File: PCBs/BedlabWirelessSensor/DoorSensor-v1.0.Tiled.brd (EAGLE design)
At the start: 43.2 x 51.1 mm, 19 parts, among them U1 ATMEGA328P_PDIP

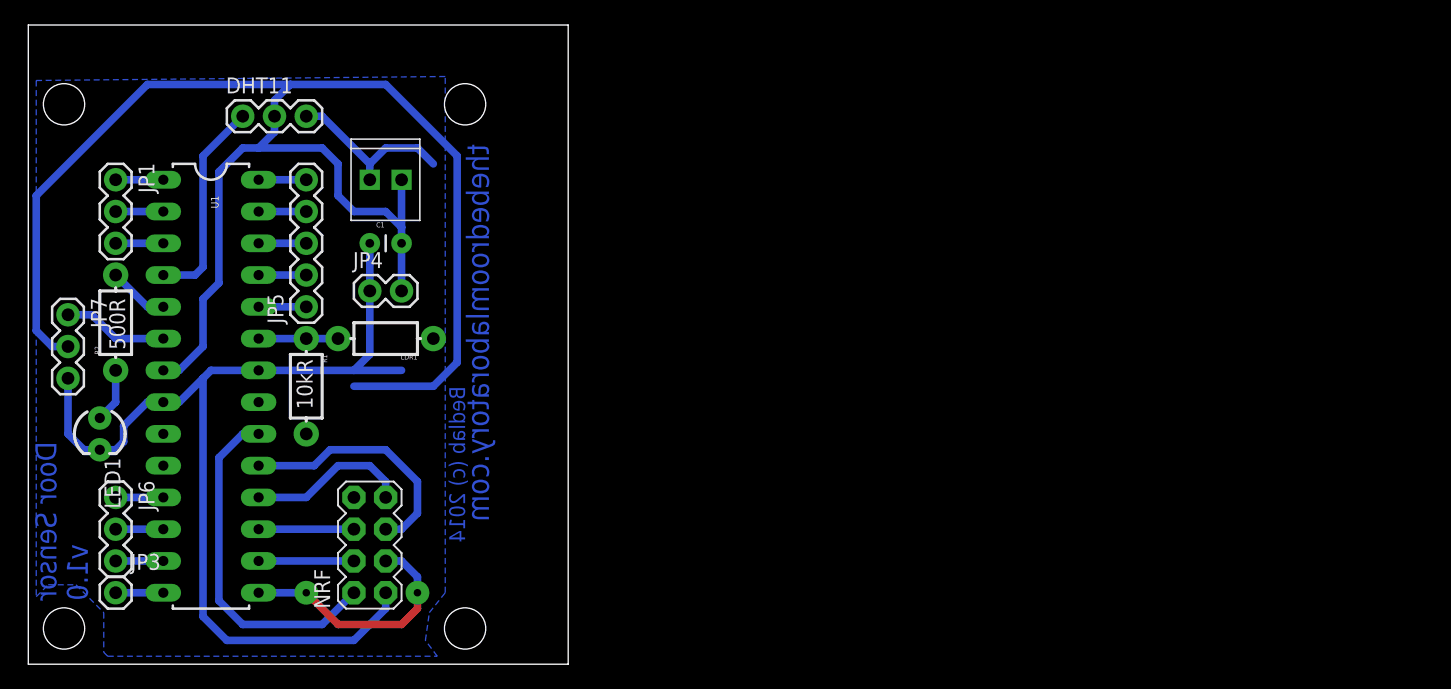
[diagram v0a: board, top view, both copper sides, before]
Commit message: Tiled PCB layout added for printing tomorrow. Additionally, changes made to arduino sketches to add funtionality for LDR, LED, Temp/humid sensor and switching the lights on/off from the gateway.
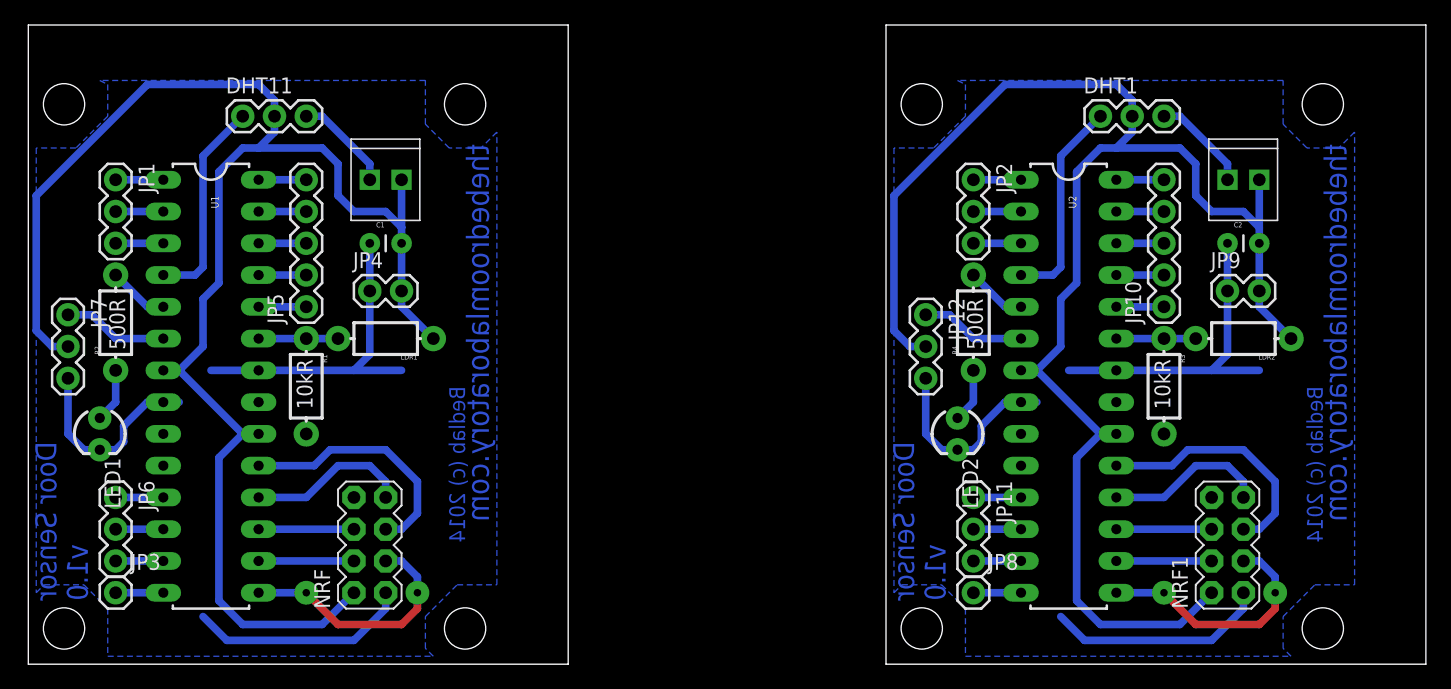
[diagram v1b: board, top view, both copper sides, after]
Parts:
- added C2: 1uF, SparkFun-Passives:CAP-PTH-SMALL
- added DHT1, JP11, JP12, JP2: (no value), SparkFun-Connectors:1X03
- added JP10: (no value), SparkFun-Connectors:1X05
- added JP8: M01PTH, SparkFun-Connectors:1X01
- added JP9: M02PTH, SparkFun-Connectors:1X02
- added LDR2: (no value), SparkFun-Passives:AXIAL-0.3-KIT
- added LED2: (no value), SparkFun-LED:LED3MM
- added NRF1: M04X2, SparkFun-Connectors:2X4
- added POWER1: M022.54MM_SCREWTERM, SparkFun-Connectors:1X02_2.54_SCREWTERM
- added R3: 10kR, SparkFun-Passives:AXIAL-0.3-KIT
- added R4: 500R, SparkFun-Passives:AXIAL-0.3-KIT
- added U$5, U$6, U$7, U$8: (no value), SparkFun-Electromechanical:STAND-OFF
- added U2: ATMEGA328P_PDIP, SparkFun-DigitalIC:DIL28-3
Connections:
- new net A10: JP10.5, U2.28
- new net A6: JP10.1, U2.24
- new net A7: JP10.2, U2.25
- new net A8: JP10.3, U2.26
- new net A9: JP10.4, U2.27
- new net D1: JP8.1, U2.14
- new net D10: JP11.3, U2.13
- new net D2: JP12.1, U2.6
- new net D3: JP11.1, U2.11
- new net D9: JP11.2, U2.12
- new net GND1: C2.1, DHT1.3, JP12.3, JP9.1, LED2.K, NRF1.1, POWER1.P2, R3.P$2, U2.22, U2.8
- new net N$11: LED2.A, R4.P$1
- new net N$12: R4.P$2, U2.5
- new net N$13: NRF1.3, U2.15
- new net N$14: NRF1.4, U2.16
- new net N$15: NRF1.5, U2.19
- new net N$16: NRF1.7, U2.18
- new net N$17: NRF1.6, U2.17
- new net N$18: DHT1.1, U2.4
- new net N$8: LDR2.P$2, R3.P$1, U2.23
- new net RESET1: JP2.1, U2.1
- new net RX1: JP2.2, U2.2
- new net TX1: JP2.3, U2.3
- new net VCC1: C2.2, DHT1.2, JP12.2, JP9.2, LDR2.P$1, NRF1.2, POWER1.P1, U2.20, U2.7
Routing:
- net VCC1: track 0.00 -> 128.4 mm
- net GND1: track 0.00 -> 67.8 mm
- net VCC: track 160.1 -> 128.4 mm
- net GND: track 96.5 -> 67.8 mm
- net N$15: track 0.00 -> 19.9 mm
- net N$13: track 0.00 -> 19.9 mm, vias 0 -> 2
- net N$18: track 0.00 -> 16.8 mm
- net N$16: track 0.00 -> 13.0 mm
- net D2: track 0.00 -> 8.41 mm
- net N$17: track 0.00 -> 7.62 mm
- net N$14: track 0.00 -> 7.62 mm
- net N$8: track 0.00 -> 6.35 mm
- net N$12: track 0.00 -> 4.86 mm
- net N$11: track 0.00 -> 4.34 mm
- net TX1: track 0.00 -> 3.81 mm
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- added copper zone on layer 16, net GND1
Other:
- board size 43.2 x 51.1 mm -> 111.7 x 51.1 mm
